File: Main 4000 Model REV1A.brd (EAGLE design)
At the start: 160 x 100 mm, 127 parts, among them CON1 HN1X30_WITHOUT(15-20), CON2 HN1X30_WITHOUT(15-20), IC1 QUAD_OPAMPD, IC2 7818TV, IC3 TL331, IC4 TUSB2036, Q1 16MHZ, Q2 TIP120, Q3 BC846, Q4 BC846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

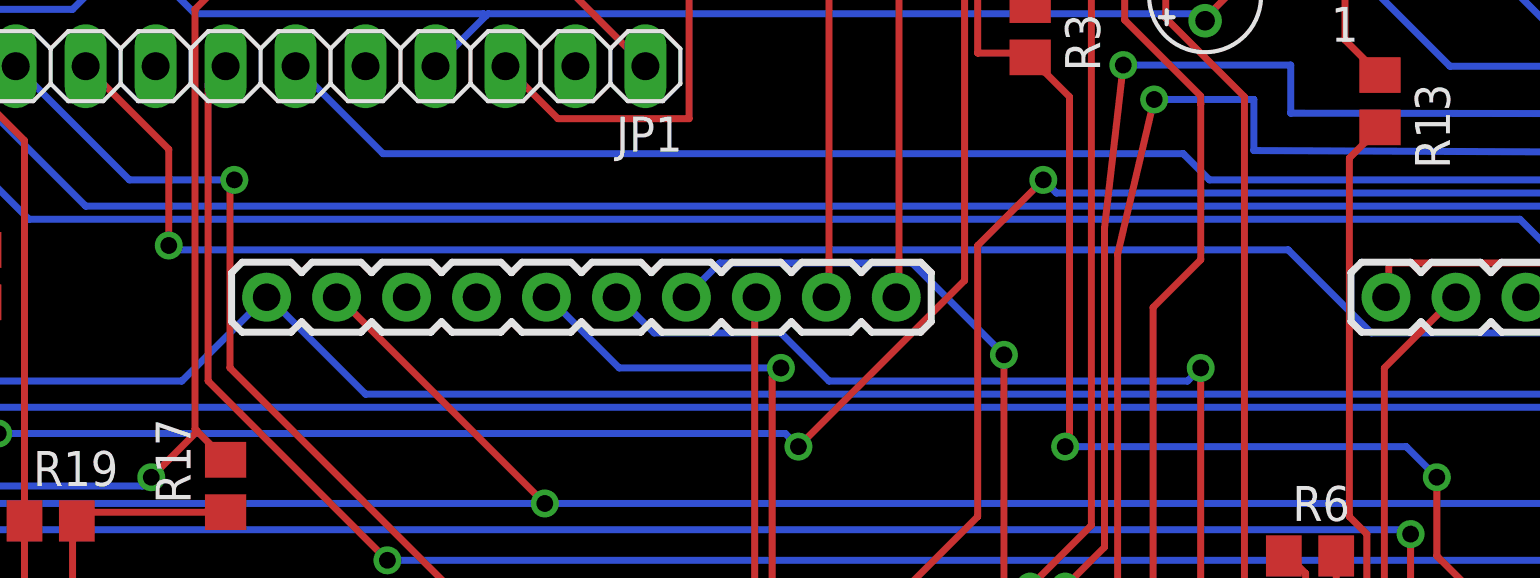
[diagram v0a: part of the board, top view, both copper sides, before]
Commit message: Routed Pi version
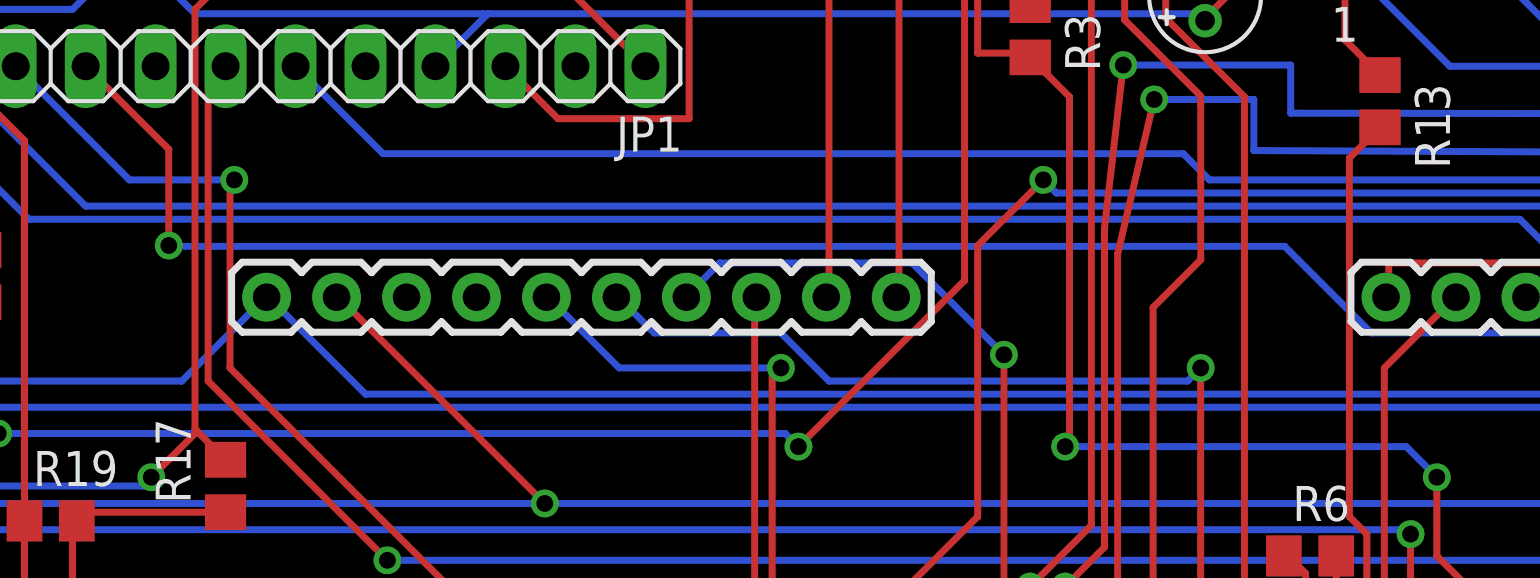
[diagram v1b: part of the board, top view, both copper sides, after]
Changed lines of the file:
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@@
 <setting verticaltext="up"/>
 </settings>
-<grid distance="0.000000123031" unitdist="inch" unit="inch" style="lines" multiple="1" display="no" altdistance="0.025" altunitdist="inch" altunit="inch"/>
+<grid distance="0.005" unitdist="inch" unit="inch" style="lines" multiple="1" display="no" altdistance="0.025" altunitdist="inch" altunit="inch"/>
 <layers>
 <layer number="1" name="Top" color="4" fill="1" visible="yes" active="yes"/>
@@
 <wire x1="55.08625" y1="52.86375" x2="52.07" y2="55.88" width="0.254" layer="1"/>
 <wire x1="55.08625" y1="49.37125" x2="55.08625" y2="52.86375" width="0.254" layer="1"/>
-<wire x1="55.245" y1="49.2125" x2="55.08625" y2="49.37125" width="0.254" layer="16"/>
-<wire x1="95.72625" y1="49.2125" x2="55.245" y2="49.2125" width="0.254" layer="16"/>
-<wire x1="98.7425" y1="46.19625" x2="95.72625" y2="49.2125" width="0.254" layer="16"/>
+<wire x1="55.245" y1="49.3395" x2="55.08625" y2="49.37125" width="0.254" layer="16"/>
+<wire x1="95.59925" y1="49.3395" x2="55.245" y2="49.3395" width="0.254" layer="16"/>
+<wire x1="98.7425" y1="46.19625" x2="95.59925" y2="49.3395" width="0.254" layer="16"/>
 <wire x1="110.64875" y1="46.19625" x2="98.7425" y2="46.19625" width="0.254" layer="16"/>
 <wire x1="111.91875" y1="47.46625" x2="110.64875" y2="46.19625" width="0.254" layer="16"/>
